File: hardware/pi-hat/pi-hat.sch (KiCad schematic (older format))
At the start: 97 parts, among them J1 PWR_IN, J10 6-8, J11 PWM0, J12 PWM1, J13 KLPX-0848A-2-B, J14 KLPX-0848A-2-R, J2 A-F, J3 40HAT, J4 G-M, J5 N-Q, J6 PANEL_PWR, J7 PANEL_CTL, J8 2-5, J9 WP, Q1 DMG2305UX, Q2 DMMT5401, Q3 DMN6075S, Q4 DMP510DL, Q5 DMN6075S, U1 CAT24C32, U10 L78L33_SOT89, U11 L78L33_SOT89, U12 PCM5122PW, U13 TSR_2-2450, U2 CM1293A, U3 CM1293A, U4 CM1293A, U5 CM1293A, U6 CM1293A, U7 CM1293A, U8 MCP23S17_SO, U9 MCP23S17_SO

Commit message: choose better Q4, D5 and R16; remove R4
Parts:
- removed R4: 10k, Resistor_SMD:R_0805_2012Metric, symbol Device:R
- D5: value 10V -> MMSZ5239B-7-F (9.1V)
- Q4: value DMP510DL -> DMP4065S
- R16: value 10k -> 5.6k
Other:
- moved on the sheet: D5
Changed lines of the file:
@@
-$EndComp
-$Comp
-L Device:Q_NMOS_GSD Q5
-U 1 1 5E15C401
-P 6700 5750
-F 0 "Q5" H 6650 5600 50  0000 L CNN
-F 1 "DMN6075S" V 6950 5550 50  0000 L CNN
-F 2 "Package_TO_SOT_SMD:SOT-23" H 6900 5850 50  0001 C CNN
-F 3 "~" H 6700 5750 50  0001 C CNN
-	1    6700 5750
-	1    0    0    -1
 $EndComp
 $Comp
@@
 	1    6250 5750
 	0    1    1    0
-$EndComp
-$Comp
-L Device:R R16
-U 1 1 5E07B779
-P 6800 5400
-F 0 "R16" H 6950 5400 50  0000 C CNN
-F 1 "10k" V 6800 5400 50  0000 C CNN
-F 2 "Resistor_SMD:R_0805_2012Metric" V 6730 5400 50  0001 C CNN
-F 3 "~" H 6800 5400 50  0001 C CNN
-	1    6800 5400
-	-1   0    0    1
 $EndComp
 Wire Wire Line
@@
 	0    1    1    0
 $EndComp
-Connection ~ 7000 5250
+Wire Wire Line
+	7650 4950 8300 4950
+Text Label 5150 4950 0    50   ~ 0
+P30V
+Text Label 8300 4950 2    50   ~ 0
+PANEL_30V_OUT
+Wire Wire Line
+	5150 4950 6800 4950
+Connection ~ 6800 4950
 Connection ~ 6800 5250
 Wire Wire Line
-	7000 5250 7450 5250
-Wire Wire Line
-	6800 5250 7000 5250
+	6800 4950 7250 4950
+Wire Wire Line
+	6800 5250 7450 5250
+$Comp
+L Device:R R16
+U 1 1 5E07B779
+P 6800 5400
+F 0 "R16" H 6950 5400 50  0000 C CNN
+F 1 "5.6k" V 6800 5400 50  0000 C CNN
+F 2 "Resistor_SMD:R_0805_2012Metric" V 6730 5400 50  0001 C CNN
+F 3 "~" H 6800 5400 50  0001 C CNN
+	1    6800 5400
+	-1   0    0    1
+$EndComp
+$Comp
+L Device:D_Zener D5
+U 1 1 5E9D3265
+P 6800 5100
+F 0 "D5" V 6754 5179 50  0000 L CNN
+F 1 "MMSZ5239B-7-F (9.1V)" V 6800 4100 50  0000 L CNN
+F 2 "Diode_SMD:D_0805_2012Metric" H 6800 5100 50  0001 C CNN
+F 3 "~" H 6800 5100 50  0001 C CNN
+	1    6800 5100
+	0    1    1    0
+$EndComp
 $Comp
 L Device:Q_PMOS_GSD Q4
@@
 P 7450 5050
 F 0 "Q4" V 7400 5150 50  0000 L CNN
-F 1 "DMP510DL" V 7700 4850 50  0000 L CNN
+F 1 "DMP4065S" V 7700 4850 50  0000 L CNN
 F 2 "Package_TO_SOT_SMD:SOT-23" H 7650 5150 50  0001 C CNN
 F 3 "~" H 7450 5050 50  0001 C CNN
@@
 	0    1    -1   0
 $EndComp
-Wire Wire Line
-	7000 4950 7250 4950
-Connection ~ 7000 4950
-$Comp
-L Device:D_Zener D5
-U 1 1 5E9D3265
-P 7000 5100
-F 0 "D5" V 6954 5179 50  0000 L CNN
-F 1 "10V" V 7045 5179 50  0000 L CNN
-F 2 "Diode_SMD:D_0805_2012Metric" H 7000 5100 50  0001 C CNN
-F 3 "~" H 7000 5100 50  0001 C CNN
-	1    7000 5100
-	0    1    1    0
-$EndComp
-Connection ~ 6800 4950
-Wire Wire Line
-	6800 4950 5150 4950
-Wire Wire Line
-	7650 4950 8300 4950
-Wire Wire Line
-	6800 4950 7000 4950
-$Comp
-L Device:R R4
-U 1 1 5F9056BF
-P 6800 5100
-F 0 "R4" H 6900 5100 50  0000 C CNN
-F 1 "10k" V 6800 5100 50  0000 C CNN
-F 2 "Resistor_SMD:R_0805_2012Metric" V 6730 5100 50  0001 C CNN
-F 3 "~" H 6800 5100 50  0001 C CNN
-	1    6800 5100
-	-1   0    0    1
-$EndComp
-Text Label 5150 4950 0    50   ~ 0
-P30V
-Text Label 8300 4950 2    50   ~ 0
-PANEL_30V_OUT
+$Comp
+L Device:Q_NMOS_GSD Q5
+U 1 1 5E15C401
+P 6700 5750
+F 0 "Q5" H 6650 5600 50  0000 L CNN
+F 1 "DMN6075S" V 6950 5550 50  0000 L CNN
+F 2 "Package_TO_SOT_SMD:SOT-23" H 6900 5850 50  0001 C CNN
+F 3 "~" H 6700 5750 50  0001 C CNN
+	1    6700 5750
+	1    0    0    -1
+$EndComp
 $EndSCHEMATC

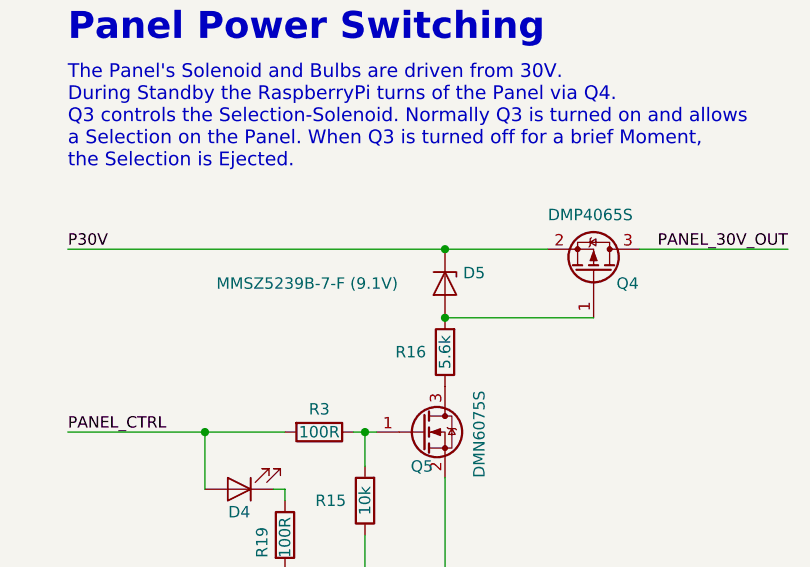
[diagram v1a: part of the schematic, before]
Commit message: add R4 as NC back
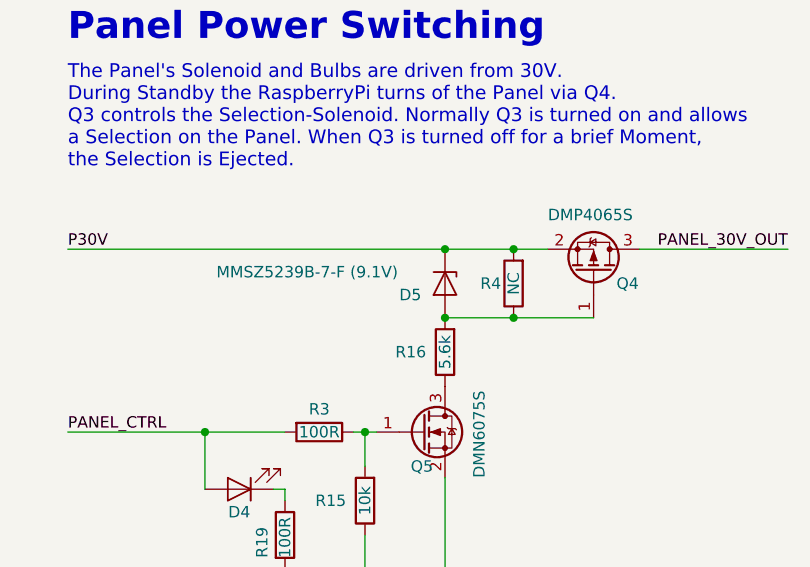
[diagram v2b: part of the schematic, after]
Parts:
- added R4: NC, Resistor_SMD:R_0805_2012Metric, symbol Device:R
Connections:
- net P30V: now also R4.2
- net at D5.2 (A), Q4.1 (G), R16.2: now also R4.1
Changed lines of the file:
@@
 Connection ~ 6800 5250
 Wire Wire Line
-	6800 4950 7250 4950
+	6800 4950 7100 4950
 Wire Wire Line
-	6800 5250 7450 5250
+	6800 5250 7100 5250
 $Comp
 L Device:R R16
@@
 U 1 1 5E9D3265
 P 6800 5100
-F 0 "D5" V 6754 5179 50  0000 L CNN
-F 1 "MMSZ5239B-7-F (9.1V)" V 6800 4100 50  0000 L CNN
+F 0 "D5" V 6850 4900 50  0000 L CNN
+F 1 "MMSZ5239B-7-F (9.1V)" V 6750 4100 50  0000 L CNN
 F 2 "Diode_SMD:D_0805_2012Metric" H 6800 5100 50  0001 C CNN
 F 3 "~" H 6800 5100 50  0001 C CNN
@@
 	1    0    0    -1
 $EndComp
+$Comp
+L Device:R R4
+U 1 1 5E2B85D4
+P 7100 5100
+F 0 "R4" H 7200 5100 50  0000 C CNN
+F 1 "NC" V 7100 5100 50  0000 C CNN
+F 2 "Resistor_SMD:R_0805_2012Metric" V 7030 5100 50  0001 C CNN
+F 3 "~" H 7100 5100 50  0001 C CNN
+	1    7100 5100
+	-1   0    0    1
+$EndComp
+Connection ~ 7100 5250
+Connection ~ 7100 4950
+Wire Wire Line
+	7100 5250 7450 5250
+Wire Wire Line
+	7100 4950 7250 4950
 $EndSCHEMATC

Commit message: documentation
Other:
- note added: "The Panel's Solenoid and Bulbs are driven from 30V.\nDuring Standby the RaspberryPi turns of the Panel via Q4 and Q5.\nD5 limits the Vgss of Q4 to 9.1V and R16 the Current across D5 to around 5mA.\n\nQ3 controls the Selection-Solenoid. Normally Q3 is turned on and allows\na Selection on the Panel. When Q3 is turned off for a brief Moment,\nthe Selection is Ejected."
- note removed: "The Panel's Solenoid and Bulbs are driven from 30V.\nDuring Standby the RaspberryPi turns of the Panel via Q4.\nQ3 controls the Selection-Solenoid. Normally Q3 is turned on and allows\na Selection on the Panel. When Q3 is turned off for a brief Moment,\nthe Selection is Ejected."
- moved on the sheet: D3, D4, D5, Q3, Q4, Q5, R1, R15, R16, R18, R19, R2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

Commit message: add 5V DC/DC Converter for LED-Strips
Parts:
- added TP8: P5V_LED0, TestPoint:TestPoint_Pad_D2.0mm, symbol Connector:TestPoint
- added TP9: P5V_LED1, TestPoint:TestPoint_Pad_D2.0mm, symbol Connector:TestPoint
- added U14, U15: TSR_2-2450, Converter_DCDC:Converter_DCDC_TRACO_TSR-1_THT, symbol Regulator_Switching:TSR_1-2450
- J1: symbol Connector:Screw_Terminal_01x02 -> Connector:Conn_01x02_Male
- J11: value PWM0 -> LED0; footprint Connector_JST:JST_XH_B2B-XH-A_1x02_P2.50mm_Vertical -> Connector_JST:JST_XH_B3B-XH-A_1x03_P2.50mm_Vertical; symbol Connector:Conn_01x02_Male -> Connector:Conn_01x03_Male
- J12: value PWM1 -> LED1; footprint Connector_JST:JST_XH_B2B-XH-A_1x02_P2.50mm_Vertical -> Connector_JST:JST_XH_B3B-XH-A_1x03_P2.50mm_Vertical; symbol Connector:Conn_01x02_Male -> Connector:Conn_01x03_Male
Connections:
- net GND: now also J1.2 (Pin_2), J11.3 (Pin_3), J12.3 (Pin_3), U14.2 (GND), U15.2 (GND); no longer J1.1 (Pin_1), J11.2 (Pin_2), J12.2 (Pin_2)
- net P30V: now also J1.1 (Pin_1), U14.1 (Vin), U15.1 (Vin); no longer J1.2 (Pin_2)
- net PWM0: now also J11.2 (Pin_2); no longer J11.1 (Pin_1)
- net PWM1: now also J12.2 (Pin_2); no longer J12.1 (Pin_1)
- new net P5V_LED0: J11.1 (Pin_1), TP8.1, U14.3 (Vout)
- new net P5V_LED1: J12.1 (Pin_1), TP9.1, U15.3 (Vout)
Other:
- note added: "RGB-LED Section"
- note removed: "PWM Connectors"
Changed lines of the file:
@@
 Text Notes 9100 8800 0    118  ~ 24
 Audio Connector
-Text Notes 850  10500 0    118  ~ 24
-PWM Connectors
-$Comp
-L Connector:Conn_01x02_Male J11
+Text Notes 9050 5800 0    118  ~ 24
+RGB-LED Section
+$Comp
+L Connector:Conn_01x03_Male J11
 U 1 1 5E4B541C
-P 900 10900
-F 0 "J11" H 1008 11081 50  0000 C CNN
-F 1 "PWM0" H 1008 10990 50  0000 C CNN
-F 2 "Connector_JST:JST_XH_B2B-XH-A_1x02_P2.50mm_Vertical" H 900 10900 50  0001 C CNN
-F 3 "~" H 900 10900 50  0001 C CNN
-	1    900  10900
-	1    0    0    -1
-$EndComp
-$Comp
-L Connector:Conn_01x02_Male J12
+P 9200 6200
+F 0 "J11" H 9300 6500 50  0000 C CNN
+F 1 "LED0" H 9300 6400 50  0000 C CNN
+F 2 "Connector_JST:JST_XH_B3B-XH-A_1x03_P2.50mm_Vertical" H 9200 6200 50  0001 C CNN
+F 3 "~" H 9200 6200 50  0001 C CNN
+	1    9200 6200
+	1    0    0    -1
+$EndComp
+$Comp
+L Connector:Conn_01x03_Male J12
 U 1 1 5E4B5B8E
-P 1700 10900
-F 0 "J12" H 1808 11081 50  0000 C CNN
-F 1 "PWM1" H 1808 10990 50  0000 C CNN
-F 2 "Connector_JST:JST_XH_B2B-XH-A_1x02_P2.50mm_Vertical" H 1700 10900 50  0001 C CNN
-F 3 "~" H 1700 10900 50  0001 C CNN
-	1    1700 10900
-	1    0    0    -1
-$EndComp
-Wire Wire Line
-	1900 10900 2300 10900
-Wire Wire Line
-	1900 11000 2050 11000
+P 10000 6200
+F 0 "J12" H 10100 6500 50  0000 C CNN
+F 1 "LED1" H 10100 6400 50  0000 C CNN
+F 2 "Connector_JST:JST_XH_B3B-XH-A_1x03_P2.50mm_Vertical" H 10000 6200 50  0001 C CNN
+F 3 "~" H 10000 6200 50  0001 C CNN
+	1    10000 6200
+	1    0    0    -1
+$EndComp
+Wire Wire Line
+	10200 6200 10600 6200
+Wire Wire Line
+	10200 6300 10350 6300
 $Comp
 L power:GND #PWR016
 U 1 1 5E4E0D9D
-P 2050 11000
-F 0 "#PWR016" H 2050 10750 50  0001 C CNN
-F 1 "GND" H 2055 10827 50  0000 C CNN
-F 2 "" H 2050 11000 50  0001 C CNN
-F 3 "" H 2050 11000 50  0001 C CNN
-	1    2050 11000
-	1    0    0    -1
-$EndComp
-Wire Wire Line
-	1100 11000 1250 11000
+P 10350 6300
+F 0 "#PWR016" H 10350 6050 50  0001 C CNN
+F 1 "GND" H 10355 6127 50  0000 C CNN
+F 2 "" H 10350 6300 50  0001 C CNN
+F 3 "" H 10350 6300 50  0001 C CNN
+	1    10350 6300
+	1    0    0    -1
+$EndComp
+Wire Wire Line
+	9400 6300 9550 6300
 $Comp
 L power:GND #PWR015
 U 1 1 5E4EC2AA
-P 1250 11000
-F 0 "#PWR015" H 1250 10750 50  0001 C CNN
-F 1 "GND" H 1255 10827 50  0000 C CNN
-F 2 "" H 1250 11000 50  0001 C CNN
-F 3 "" H 1250 11000 50  0001 C CNN
-	1    1250 11000
-	1    0    0    -1
-$EndComp
-Wire Wire Line
-	1100 10900 1500 10900
-Text Label 1500 10900 2    50   ~ 0
+P 9550 6300
+F 0 "#PWR015" H 9550 6050 50  0001 C CNN
+F 1 "GND" H 9555 6127 50  0000 C CNN
+F 2 "" H 9550 6300 50  0001 C CNN
+F 3 "" H 9550 6300 50  0001 C CNN
+	1    9550 6300
+	1    0    0    -1
+$EndComp
+Wire Wire Line
+	9400 6200 9800 6200
+Text Label 9800 6200 2    50   ~ 0
 PWM0
 $Comp
@@
 Wire Wire Line
 	4350 2250 3150 2250
-Text Label 2300 10900 2    50   ~ 0
+Text Label 10600 6200 2    50   ~ 0
 PWM1
 Wire Wire Line
@@
 Wire Wire Line
 	9650 2450 10050 2450
-$Comp
-L Device:Jumper_NO_Small JP2
-U 1 1 5DFD09F1
-P 5250 9800
-F 0 "JP2" V 5250 9848 50  0000 L CNN
-F 1 "Jumper_NO_Small" V 5295 9848 50  0001 L CNN
-F 2 "Jumper:SolderJumper-2_P1.3mm_Open_Pad1.0x1.5mm" H 5250 9800 50  0001 C CNN
-F 3 "~" H 5250 9800 50  0001 C CNN
-	1    5250 9800
-	0    1    1    0
-$EndComp
 Wire Wire Line
 	5500 9750 5500 9700
 Wire Wire Line
-	5500 9700 5250 9700
-Wire Wire Line
 	5500 9750 6300 9750
-Wire Wire Line
-	5250 9900 5500 9900
 Wire Wire Line
 	5500 9900 5500 9850
@@
 $EndComp
 $Comp
-L Connector:Screw_Terminal_01x02 J1
+L Connector:Conn_01x02_Male J1
 U 1 1 5E92A759
-P 9450 2550
-F 0 "J1" H 9368 2225 50  0000 C CNN
-F 1 "PWR_IN" H 9368 2316 50  0000 C CNN
-F 2 "" H 9450 2550 50  0001 C CNN
-F 3 "~" H 9450 2550 50  0001 C CNN
-	1    9450 2550
-	-1   0    0    1
+P 9450 2450
+F 0 "J1" H 9550 2100 50  0000 C CNN
+F 1 "PWR_IN" H 9550 2200 50  0000 C CNN
+F 2 "" H 9450 2450 50  0001 C CNN
+F 3 "~" H 9450 2450 50  0001 C CNN
+	1    9450 2450
+	1    0    0    -1
 $EndComp
 Wire Wire Line
@@
 Wire Wire Line
 	7150 5150 7300 5150
+Text Label 10700 6900 2    50   ~ 0
+P5V_LED0
+$Comp
+L Connector:TestPoint TP8
+U 1 1 5E4A77B3
+P 10250 7050
+F 0 "TP8" V 10204 7238 50  0000 L CNN
+F 1 "P5V_LED0" V 10295 7238 50  0000 L CNN
+F 2 "TestPoint:TestPoint_Pad_D2.0mm" H 10450 7050 50  0001 C CNN
+F 3 "~" H 10450 7050 50  0001 C CNN
+	1    10250 7050
+	0    1    1    0
+$EndComp
+$Comp
+L Regulator_Switching:TSR_1-2450 U14
+U 1 1 5E4A77B9
+P 9850 7000
+F 0 "U14" H 9850 7367 50  0000 C CNN
+F 1 "TSR_2-2450" H 9850 7276 50  0000 C CNN
+F 2 "Converter_DCDC:Converter_DCDC_TRACO_TSR-1_THT" H 9850 6850 50  0001 L CIN
+F 3 "http://www.tracopower.com/products/tsr1.pdf" H 9850 7000 50  0001 C CNN
+	1    9850 7000
+	1    0    0    -1
+$EndComp
+Wire Wire Line
+	10250 6900 10700 6900
+Wire Wire Line
+	9450 6900 9200 6900
+Text Label 9200 6900 0    50   ~ 0
+P30V
+$Comp
+L power:GND #PWR0127
+U 1 1 5E4A77C2
+P 9850 7200
+F 0 "#PWR0127" H 9850 6950 50  0001 C CNN
+F 1 "GND" H 9855 7027 50  0000 C CNN
+F 2 "" H 9850 7200 50  0001 C CNN
+F 3 "" H 9850 7200 50  0001 C CNN
+	1    9850 7200
+	1    0    0    -1
+$EndComp
+Wire Wire Line
+	10250 6900 10250 7050
+Connection ~ 10250 6900
+Wire Wire Line
+	9400 6100 9800 6100
+Wire Wire Line
+	10200 6100 10600 6100
+Text Label 9800 6100 2    50   ~ 0
+P5V_LED0
+Text Label 10600 6100 2    50   ~ 0
+P5V_LED1
+Text Label 10700 7850 2    50   ~ 0
+P5V_LED1
+$Comp
+L Connector:TestPoint TP9
+U 1 1 5E6661C1
+P 10250 8000
+F 0 "TP9" V 10204 8188 50  0000 L CNN
+F 1 "P5V_LED1" V 10295 8188 50  0000 L CNN
+F 2 "TestPoint:TestPoint_Pad_D2.0mm" H 10450 8000 50  0001 C CNN
+F 3 "~" H 10450 8000 50  0001 C CNN
+	1    10250 8000
+	0    1    1    0
+$EndComp
+$Comp
+L Regulator_Switching:TSR_1-2450 U15
+U 1 1 5E6661C7
+P 9850 7950
+F 0 "U15" H 9850 8317 50  0000 C CNN
+F 1 "TSR_2-2450" H 9850 8226 50  0000 C CNN
+F 2 "Converter_DCDC:Converter_DCDC_TRACO_TSR-1_THT" H 9850 7800 50  0001 L CIN
+F 3 "http://www.tracopower.com/products/tsr1.pdf" H 9850 7950 50  0001 C CNN
+	1    9850 7950
+	1    0    0    -1
+$EndComp
+Wire Wire Line
+	10250 7850 10700 7850
+Wire Wire Line
+	9450 7850 9200 7850
+Text Label 9200 7850 0    50   ~ 0
+P30V
+$Comp
+L power:GND #PWR0128
+U 1 1 5E6661D0
+P 9850 8150
+F 0 "#PWR0128" H 9850 7900 50  0001 C CNN
+F 1 "GND" H 9855 7977 50  0000 C CNN
+F 2 "" H 9850 8150 50  0001 C CNN
+F 3 "" H 9850 8150 50  0001 C CNN
+	1    9850 8150
+	1    0    0    -1
+$EndComp
+Wire Wire Line
+	10250 7850 10250 8000
+Connection ~ 10250 7850
+Wire Wire Line
+	5250 9900 5500 9900
+Wire Wire Line
+	5500 9700 5250 9700
+$Comp
+L Device:Jumper_NO_Small JP2
+U 1 1 5DFD09F1
+P 5250 9800
+F 0 "JP2" V 5250 9848 50  0000 L CNN
+F 1 "Jumper_NO_Small" V 5295 9848 50  0001 L CNN
+F 2 "Jumper:SolderJumper-2_P1.3mm_Open_Pad1.0x1.5mm" H 5250 9800 50  0001 C CNN
+F 3 "~" H 5250 9800 50  0001 C CNN
+	1    5250 9800
+	0    1    1    0
+$EndComp
 $EndSCHEMATC

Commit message: shrink testpoints and sot-6 footprint
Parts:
- J1: footprint (none) -> TerminalBlock:TerminalBlock_bornier-2_P5.08mm
- Q2: footprint Package_TO_SOT_SMD:SOT-23-6_Handsoldering -> Package_TO_SOT_SMD:SOT-23-6
- TP1, TP2, TP3, TP4, TP5, TP6, TP7, TP8, TP9: footprint TestPoint:TestPoint_Pad_D2.0mm -> TestPoint:TestPoint_Pad_D1.5mm
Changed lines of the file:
@@
 F 0 "Q2" H 7100 2575 50  0000 L CNN
 F 1 "DMMT5401" H 7100 2500 50  0000 L CNN
-F 2 "Package_TO_SOT_SMD:SOT-23-6_Handsoldering" H 7100 2425 50  0001 L CIN
+F 2 "Package_TO_SOT_SMD:SOT-23-6" H 7100 2425 50  0001 L CIN
 F 3 "" H 6900 2500 50  0000 L CNN
 	2    6900 2500
@@
 F 0 "Q2" H 6500 2575 50  0000 L CNN
 F 1 "DMMT5401" H 6500 2500 50  0000 L CNN
-F 2 "Package_TO_SOT_SMD:SOT-23-6_Handsoldering" H 6500 2425 50  0001 L CIN
+F 2 "Package_TO_SOT_SMD:SOT-23-6" H 6500 2425 50  0001 L CIN
 F 3 "" H 6300 2500 50  0000 L CNN
 	1    6300 2500
@@
 F 0 "TP3" V 12454 2838 50  0000 L CNN
 F 1 "P5V" V 12545 2838 50  0000 L CNN
-F 2 "TestPoint:TestPoint_Pad_D2.0mm" H 12700 2650 50  0001 C CNN
+F 2 "TestPoint:TestPoint_Pad_D1.5mm" H 12700 2650 50  0001 C CNN
 F 3 "~" H 12700 2650 50  0001 C CNN
 	1    12500 2650
@@
 F 0 "TP1" V 7254 2238 50  0000 L CNN
 F 1 "P5V_HAT" V 7345 2238 50  0000 L CNN
-F 2 "TestPoint:TestPoint_Pad_D2.0mm" H 7500 2050 50  0001 C CNN
+F 2 "TestPoint:TestPoint_Pad_D1.5mm" H 7500 2050 50  0001 C CNN
 F 3 "~" H 7500 2050 50  0001 C CNN
 	1    7300 2050
@@
 F 0 "TP4" V 12354 3788 50  0000 L CNN
 F 1 "P3V3" V 12445 3788 50  0000 L CNN
-F 2 "TestPoint:TestPoint_Pad_D2.0mm" H 12600 3600 50  0001 C CNN
+F 2 "TestPoint:TestPoint_Pad_D1.5mm" H 12600 3600 50  0001 C CNN
 F 3 "~" H 12600 3600 50  0001 C CNN
 	1    12400 3600
@@
 F 0 "TP5" V 12354 4688 50  0000 L CNN
 F 1 "P3V3A" V 12445 4688 50  0000 L CNN
-F 2 "TestPoint:TestPoint_Pad_D2.0mm" H 12600 4500 50  0001 C CNN
+F 2 "TestPoint:TestPoint_Pad_D1.5mm" H 12600 4500 50  0001 C CNN
 F 3 "~" H 12600 4500 50  0001 C CNN
 	1    12400 4500
@@
 F 0 "J1" H 9550 2100 50  0000 C CNN
 F 1 "PWR_IN" H 9550 2200 50  0000 C CNN
-F 2 "" H 9450 2450 50  0001 C CNN
+F 2 "TerminalBlock:TerminalBlock_bornier-2_P5.08mm" H 9450 2450 50  0001 C CNN
 F 3 "~" H 9450 2450 50  0001 C CNN
 	1    9450 2450
@@
 F 0 "TP6" V 10154 4488 50  0000 L CNN
 F 1 "GNDA" V 10245 4488 50  0000 L CNN
-F 2 "TestPoint:TestPoint_Pad_D2.0mm" H 10400 4300 50  0001 C CNN
+F 2 "TestPoint:TestPoint_Pad_D1.5mm" H 10400 4300 50  0001 C CNN
 F 3 "~" H 10400 4300 50  0001 C CNN
 	1    10200 4300
@@
 F 0 "TP2" V 9654 4488 50  0000 L CNN
 F 1 "GND" V 9745 4488 50  0000 L CNN
-F 2 "TestPoint:TestPoint_Pad_D2.0mm" H 9900 4300 50  0001 C CNN
+F 2 "TestPoint:TestPoint_Pad_D1.5mm" H 9900 4300 50  0001 C CNN
 F 3 "~" H 9900 4300 50  0001 C CNN
 	1    9700 4300
@@
 F 0 "TP7" V 10004 2488 50  0000 L CNN
 F 1 "P30V" V 10095 2488 50  0000 L CNN
-F 2 "TestPoint:TestPoint_Pad_D2.0mm" H 10250 2300 50  0001 C CNN
+F 2 "TestPoint:TestPoint_Pad_D1.5mm" H 10250 2300 50  0001 C CNN
 F 3 "~" H 10250 2300 50  0001 C CNN
 	1    10050 2300
@@
 F 0 "TP8" V 10204 7238 50  0000 L CNN
 F 1 "P5V_LED0" V 10295 7238 50  0000 L CNN
-F 2 "TestPoint:TestPoint_Pad_D2.0mm" H 10450 7050 50  0001 C CNN
+F 2 "TestPoint:TestPoint_Pad_D1.5mm" H 10450 7050 50  0001 C CNN
 F 3 "~" H 10450 7050 50  0001 C CNN
 	1    10250 7050
@@
 F 0 "TP9" V 10204 8188 50  0000 L CNN
 F 1 "P5V_LED1" V 10295 8188 50  0000 L CNN
-F 2 "TestPoint:TestPoint_Pad_D2.0mm" H 10450 8000 50  0001 C CNN
+F 2 "TestPoint:TestPoint_Pad_D1.5mm" H 10450 8000 50  0001 C CNN
 F 3 "~" H 10450 8000 50  0001 C CNN
 	1    10250 8000

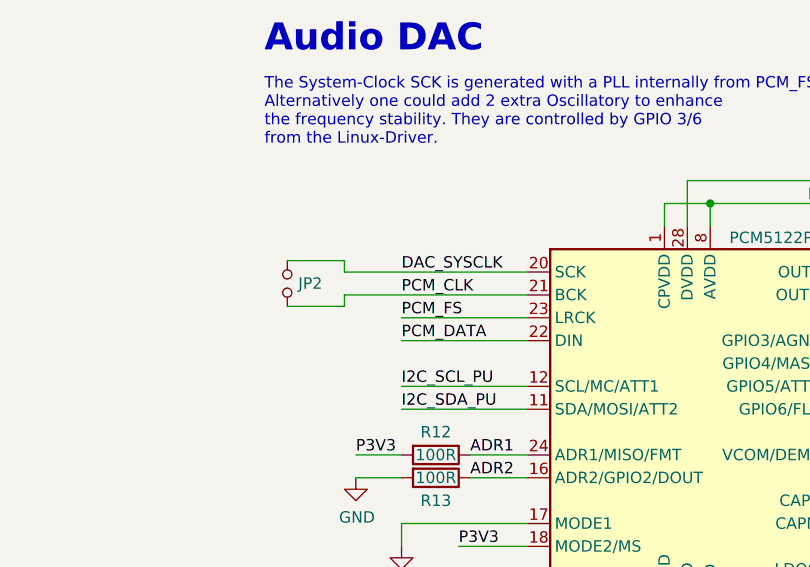
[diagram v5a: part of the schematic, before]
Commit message: remove sck/fs bridge option
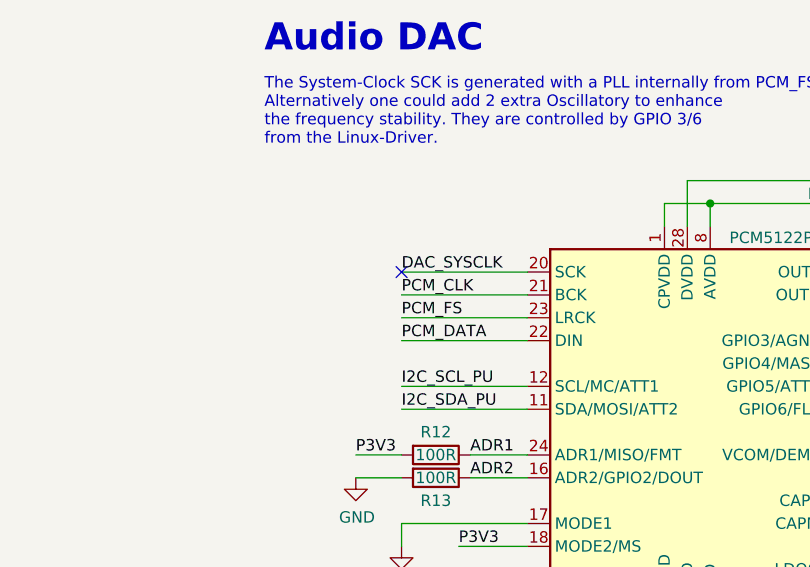
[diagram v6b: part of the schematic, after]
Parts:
- removed JP2: Jumper_NO_Small, Jumper:SolderJumper-2_P1.3mm_Open_Pad1.0x1.5mm, symbol Device:Jumper_NO_Small
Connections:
- no-connect marks 25 -> 26
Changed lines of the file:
@@
 Wire Wire Line
 	9650 2450 10050 2450
-Wire Wire Line
-	5500 9750 5500 9700
-Wire Wire Line
-	5500 9750 6300 9750
-Wire Wire Line
-	5500 9900 5500 9850
-Wire Wire Line
-	5500 9850 6300 9850
 Text Label 5150 5950 0    50   ~ 0
 PANEL_CTRL
@@
 Connection ~ 10250 7850
 Wire Wire Line
-	5250 9900 5500 9900
-Wire Wire Line
-	5500 9700 5250 9700
-$Comp
-L Device:Jumper_NO_Small JP2
-U 1 1 5DFD09F1
-P 5250 9800
-F 0 "JP2" V 5250 9848 50  0000 L CNN
-F 1 "Jumper_NO_Small" V 5295 9848 50  0001 L CNN
-F 2 "Jumper:SolderJumper-2_P1.3mm_Open_Pad1.0x1.5mm" H 5250 9800 50  0001 C CNN
-F 3 "~" H 5250 9800 50  0001 C CNN
-	1    5250 9800
-	0    1    1    0
-$EndComp
+	6300 9750 5750 9750
+Wire Wire Line
+	6300 9850 5750 9850
+NoConn ~ 5750 9750
 $EndSCHEMATC
